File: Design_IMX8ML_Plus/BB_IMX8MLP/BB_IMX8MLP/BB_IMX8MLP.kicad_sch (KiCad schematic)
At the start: 0 parts

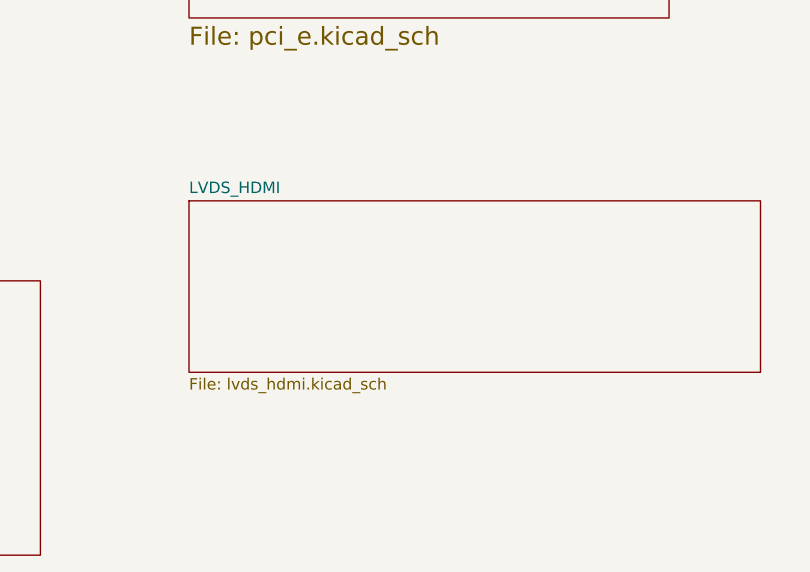
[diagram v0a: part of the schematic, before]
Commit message: Add SPB228 WIFI/BLE module
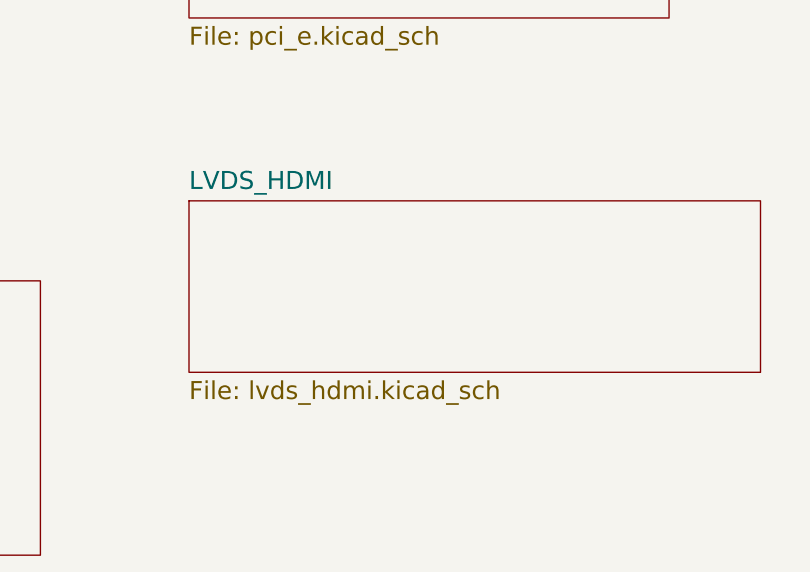
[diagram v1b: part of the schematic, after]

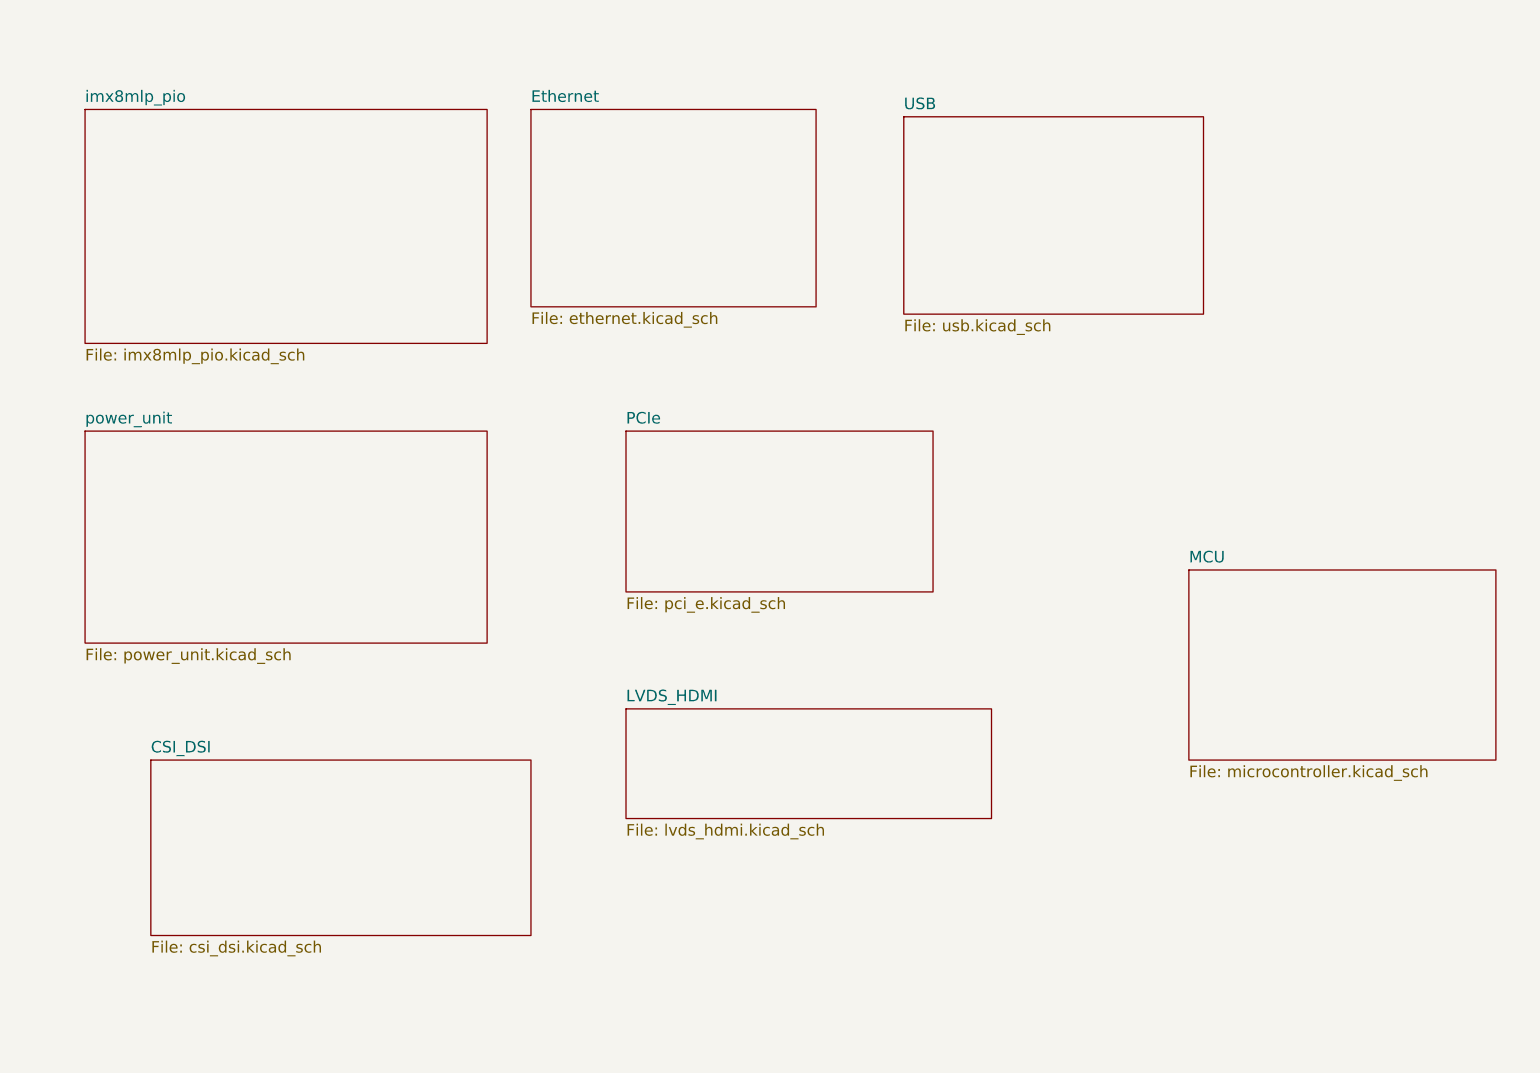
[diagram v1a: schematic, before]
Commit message: improving Ethernet, USB and Camera inteface
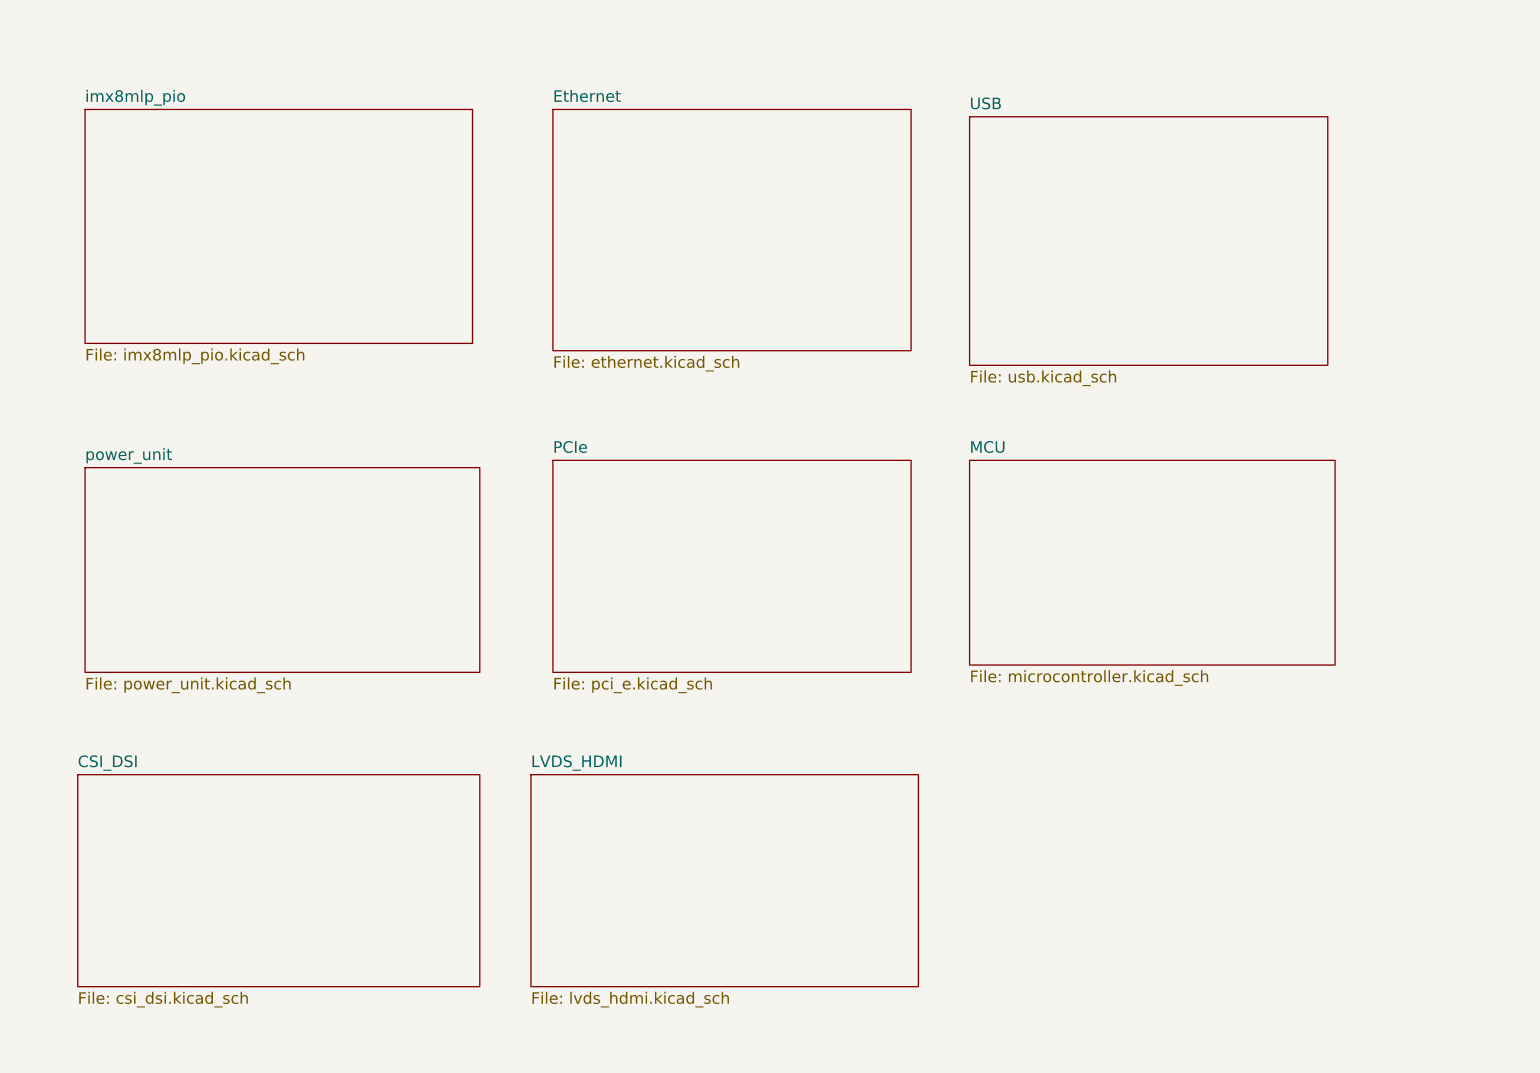
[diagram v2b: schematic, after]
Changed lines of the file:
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@@
 	(paper "A4")
 	(sheet
-		(at 107.95 30.48)
-		(size 49.53 34.29)
+		(at 111.76 30.48)
+		(size 62.23 41.91)
 		(fields_autoplaced yes)
 		(stroke
@@
 		)
 		(property "Sheetname" "Ethernet"
-			(at 107.95 29.4034 0)
+			(at 111.76 29.4034 0)
 			(effects
 				(font
@@
 		)
 		(property "Sheetfile" "ethernet.kicad_sch"
-			(at 107.95 65.6466 0)
+			(at 111.76 73.2666 0)
 			(effects
 				(font
@@
 	)
 	(sheet
-		(at 30.48 86.36)
-		(size 69.85 36.83)
+		(at 30.48 92.71)
+		(size 68.58 35.56)
 		(fields_autoplaced yes)
 		(stroke
@@
 		)
 		(property "Sheetname" "power_unit"
-			(at 30.48 85.2834 0)
+			(at 30.48 91.6334 0)
 			(effects
 				(font
@@
 		)
 		(property "Sheetfile" "power_unit.kicad_sch"
-			(at 30.48 124.0666 0)
+			(at 30.48 129.1466 0)
 			(effects
 				(font
@@
 	(sheet
 		(at 30.48 30.48)
-		(size 69.85 40.64)
+		(size 67.31 40.64)
 		(fields_autoplaced yes)
 		(stroke
@@
 	)
 	(sheet
-		(at 222.25 110.49)
-		(size 53.34 33.02)
+		(at 184.15 91.44)
+		(size 63.5 35.56)
 		(fields_autoplaced yes)
 		(stroke
@@
 		)
 		(property "Sheetname" "MCU"
-			(at 222.25 109.4134 0)
+			(at 184.15 90.3634 0)
 			(effects
 				(font
@@
 		)
 		(property "Sheetfile" "microcontroller.kicad_sch"
-			(at 222.25 144.3866 0)
+			(at 184.15 127.8766 0)
 			(effects
 				(font
@@
 	)
 	(sheet
-		(at 41.91 143.51)
-		(size 66.04 30.48)
+		(at 29.21 146.05)
+		(size 69.85 36.83)
 		(fields_autoplaced yes)
 		(stroke
@@
 		)
 		(property "Sheetname" "CSI_DSI"
-			(at 41.91 142.4334 0)
+			(at 29.21 144.9734 0)
 			(effects
 				(font
@@
 		)
 		(property "Sheetfile" "csi_dsi.kicad_sch"
-			(at 41.91 174.8666 0)
+			(at 29.21 183.7566 0)
 			(effects
 				(font
@@
 	)
 	(sheet
-		(at 172.72 31.75)
-		(size 52.07 34.29)
+		(at 184.15 31.75)
+		(size 62.23 43.18)
 		(fields_autoplaced yes)
 		(stroke
@@
 		)
 		(property "Sheetname" "USB"
-			(at 172.72 30.6734 0)
+			(at 184.15 30.6734 0)
 			(effects
 				(font
@@
 		)
 		(property "Sheetfile" "usb.kicad_sch"
-			(at 172.72 66.9166 0)
+			(at 184.15 75.8066 0)
 			(effects
 				(font
@@
 	)
 	(sheet
-		(at 124.46 86.36)
-		(size 53.34 27.94)
+		(at 111.76 91.44)
+		(size 62.23 36.83)
 		(fields_autoplaced yes)
 		(stroke
@@
 		)
 		(property "Sheetname" "PCIe"
-			(at 124.46 85.2834 0)
+			(at 111.76 90.3634 0)
 			(effects
 				(font
@@
 		)
 		(property "Sheetfile" "pci_e.kicad_sch"
-			(at 124.46 115.1766 0)
+			(at 111.76 129.1466 0)
 			(effects
 				(font
@@
 	)
 	(sheet
-		(at 124.46 134.62)
-		(size 63.5 19.05)
+		(at 107.95 146.05)
+		(size 67.31 36.83)
 		(fields_autoplaced yes)
 		(stroke
@@
 		)
 		(property "Sheetname" "LVDS_HDMI"
-			(at 124.46 133.5434 0)
+			(at 107.95 144.9734 0)
 			(effects
 				(font
@@
 		)
 		(property "Sheetfile" "lvds_hdmi.kicad_sch"
-			(at 124.46 154.5466 0)
-			(effects
-				(font
+			(at 107.95 183.7566 0)
+			(effects
+				(font

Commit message: Add LVDs and CSI Interface
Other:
- added sheet Audio (audio.kicad_sch)
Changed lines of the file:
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@@
+	)
+	(sheet
+		(at 195.58 139.7)
+		(size 64.77 20.32)
+		(fields_autoplaced yes)
+		(stroke
+			(width 0.1524)
+			(type solid)
+		)
+		(fill
+			(color 0 0 0 0.0000)
+		)
+		(property "Sheetname" "Audio"
+			(at 195.58 138.6234 0)
+			(effects
+				(font
+					(size 2 2)
+				)
+				(justify left bottom)
+			)
+		)
+		(property "Sheetfile" "audio.kicad_sch"
+			(at 195.58 160.8966 0)
+			(effects
+				(font
+					(size 2 2)
+				)
+				(justify left top)
+			)
+		)
+		(instances
+			(project "BB_IMX8MLP"
+				(path "/cd2fb234-91e5-476f-84ed-38419b628dc6"
+					(page "13")
+				)
+			)
+		)
 	)
 	(sheet
